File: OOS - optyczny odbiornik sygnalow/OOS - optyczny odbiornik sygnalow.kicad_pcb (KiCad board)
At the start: 2 copper layers, 72 x 79.5 mm, 124 parts, among them J1 Conn_01x02_Pin, J4 Conn_01x02_Socket, J5 Conn_Coaxial, J6 USB_C_Receptacle, Q1 SI2301CDS-T1-GE3, Q2 AOSS32334C, Q3 AOSS32334C, SW1 SW_Rotary_1x8_MP, U1 OPA300AIDBVR, U2 OPA300AIDBVR, U3 AP3015KTR-G1, U4 MCP73831T-2ATI/OT, U5 AP9101CAK6-ANTRG1, U6 AP2126K-ADJTRG1

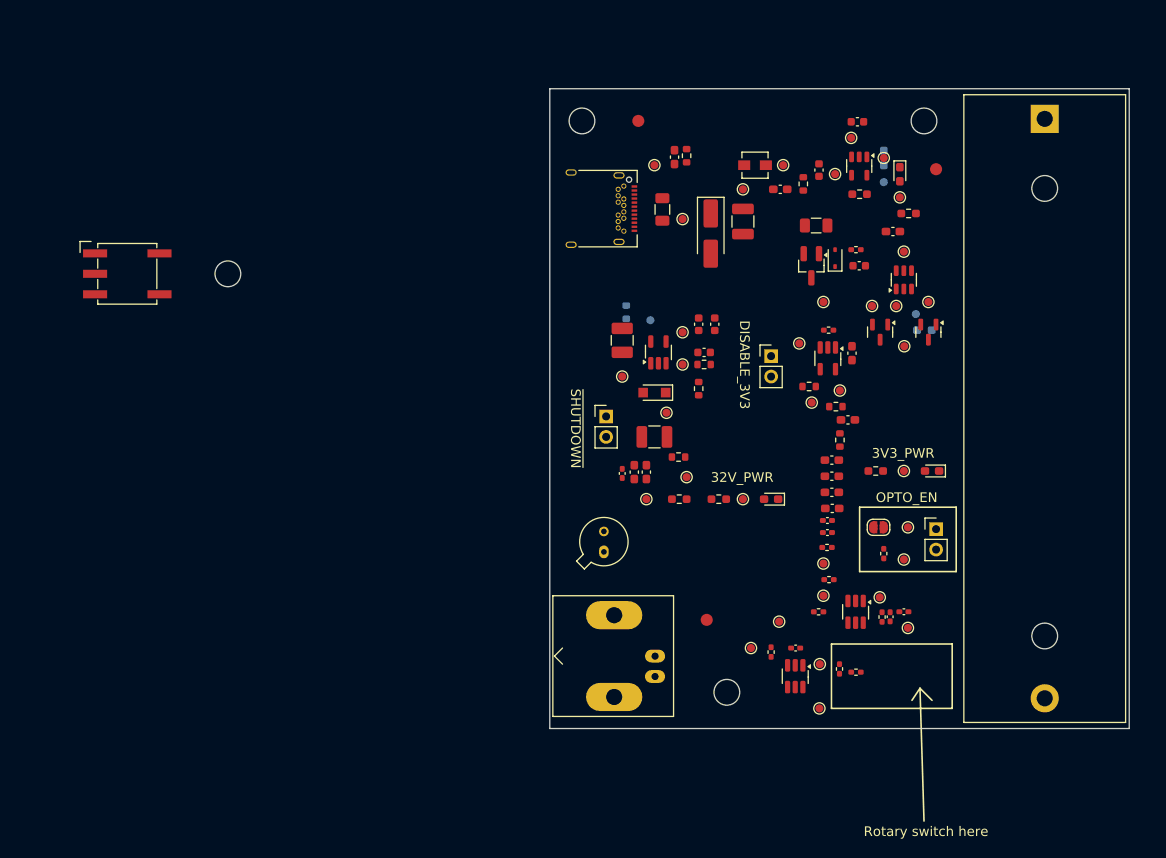
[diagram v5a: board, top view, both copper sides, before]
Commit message: Changing the placement - opamps closer to photodiode, passive components closer to ICs like DCDC converter, Linear 3v3 converter. SHDN resistor moved further away from DCDC and will be routed on the bottom layer
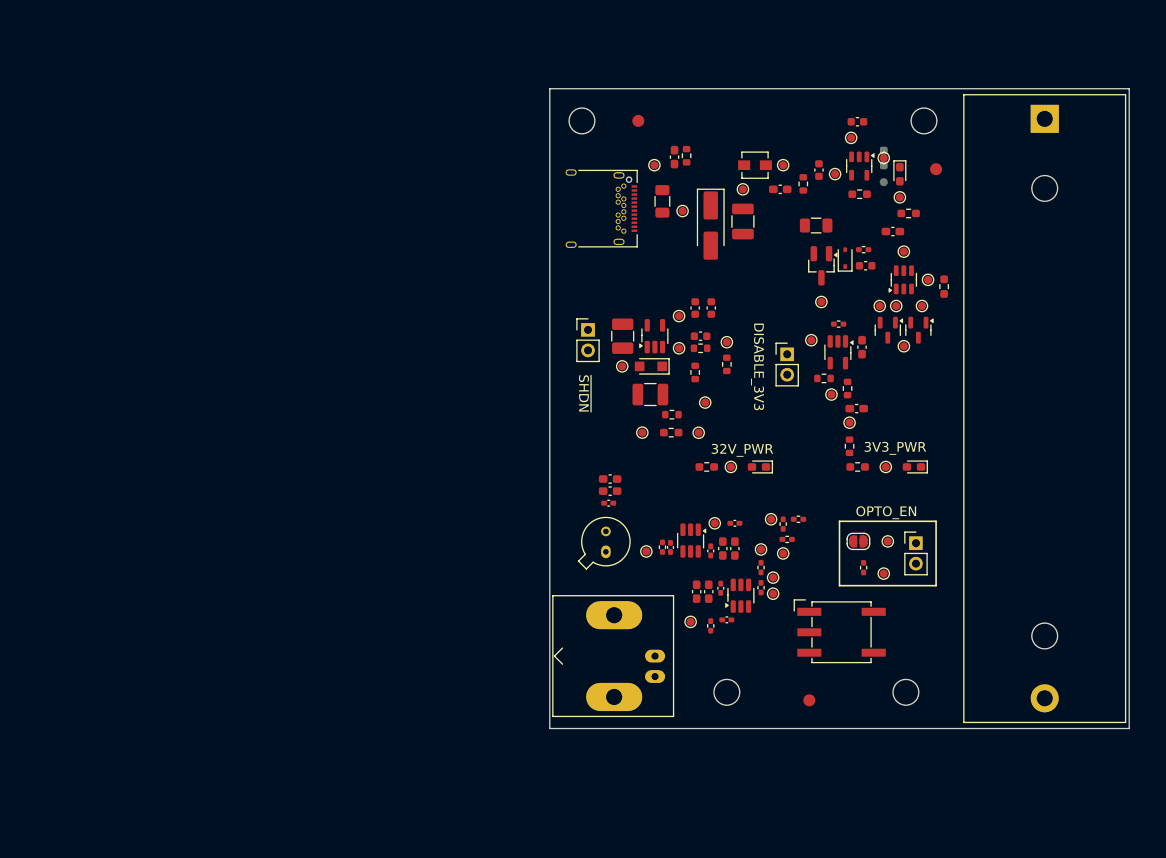
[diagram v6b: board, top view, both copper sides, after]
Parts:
- R13, R17, TP16, TP25: moved to F.Cu
- moved SW1 99.3 mm to (234.7, 95.9)
- moved H3 80.9 mm to (220.4, 103.4)
- moved R8 28.6 mm to (212.4, 85.3)
- moved C10 28.6 mm to (213.4, 85.4)
- moved C11 23.7 mm to (221.4, 82.4)
- moved TP7 22.5 mm to (218.9, 82.4)
- moved U1 22.3 mm to (215.9, 84.5)
- moved H4 22.2 mm to (242.7, 103.4)
- moved C2 22.1 mm to (216.7, 90.9), turned to -90 degrees
- moved TP8 20.7 mm to (224.7, 85.6)
- moved TP6 18.7 mm to (210.4, 85.9)
- moved C4 18.5 mm to (218.2, 90.9), turned to -90 degrees
- moved R9 17.6 mm to (224.7, 87.9), turned to -90 degrees
- moved TP9 17.2 mm to (226.2, 89.1)
- moved C1 16.3 mm to (221.4, 85.5), turned to 90 degrees
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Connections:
- R2 pad 1: Net-(U6-V_{OUT}) -> +3V3
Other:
- board text added: "~{SHDN}"
- board text removed: "~{SHUTDOWN}"

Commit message: repeated push
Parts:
- moved C25 6.58 mm to (207.4, 35.9)
- moved R26 6.55 mm to (208.9, 35.9)
- moved TP38 6.08 mm to (205.4, 36.9)
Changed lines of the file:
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@@
 			(psa4output no)
 			(plot_black_and_white yes)
-			(plotinvisibletext no)
 			(sketchpadsonfab no)
 			(plotpadnumbers no)
@@
 	(footprint "Resistor_SMD:R_0603_1608Metric"
 		(layer "F.Cu")
-		(at 215.42 36.705 90)
+		(at 208.92 35.88 90)
 		(descr "Resistor SMD 0603 (1608 Metric), square (rectangular) end terminal, IPC-7351 nominal, (Body size source: IPC-SM-782 page 72, https://www.pcb-3d.com/wordpress/wp-content/uploads/ipc-sm-782a_amendment_1_and_2.pdf), generated with kicad-footprint-generator")
 		(tags "resistor")
@@
 	(footprint "Capacitor_SMD:C_0603_1608Metric_Pad1.08x0.95mm_HandSolder"
 		(layer "F.Cu")
-		(at 213.92 36.88 90)
+		(at 207.42 35.88 90)
 		(descr "Capacitor SMD 0603 (1608 Metric), square (rectangular) end terminal, IPC-7351 nominal with elongated pad for handsoldering. (Body size source: IPC-SM-782 page 76, https://www.pcb-3d.com/wordpress/wp-content/uploads/ipc-sm-782a_amendment_1_and_2.pdf), generated with kicad-footprint-generator")
 		(tags "capacitor handsolder")
@@
 	(footprint "TestPoint:TestPoint_Pad_D1.0mm"
 		(layer "F.Cu")
-		(at 211.42 37.88)
+		(at 205.42 36.88)
 		(descr "SMD pad as test Point, diameter 1.0mm")
 		(tags "test point SMD pad")

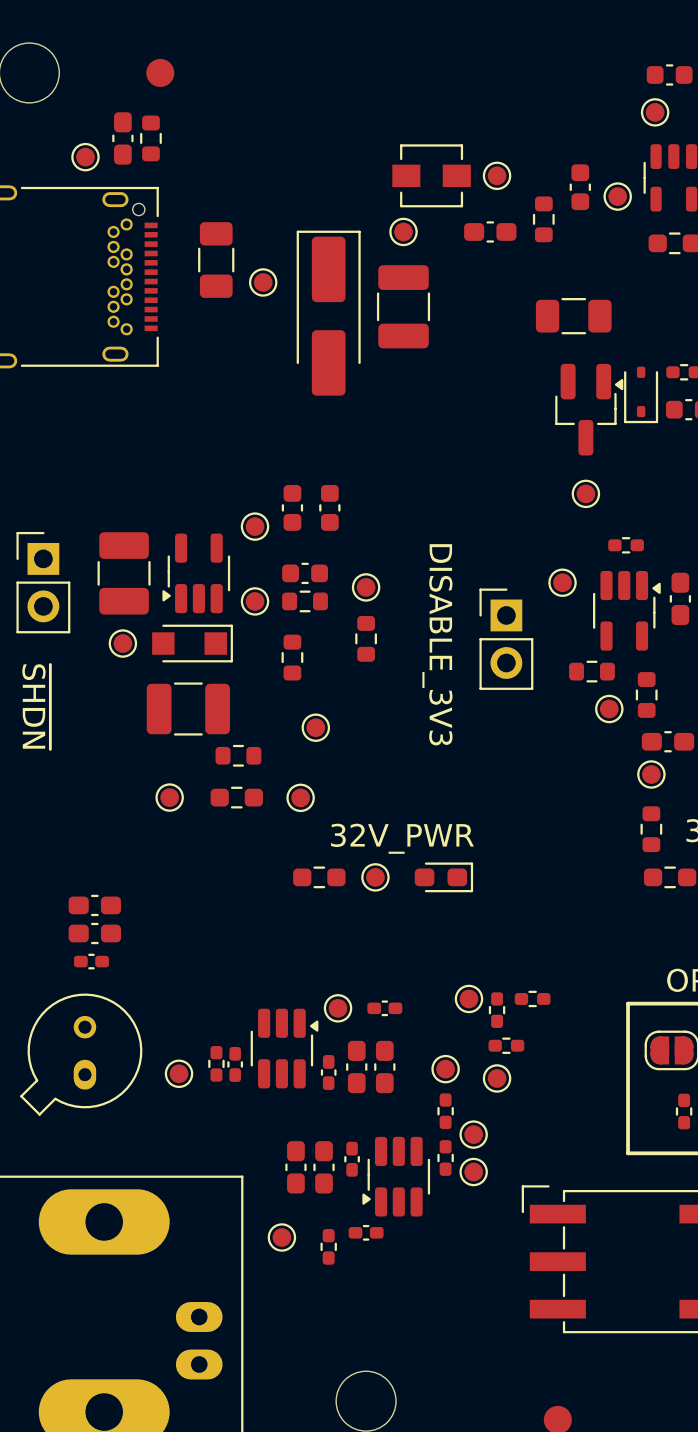
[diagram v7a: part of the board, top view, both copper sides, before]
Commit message: making opto circuit much tighter
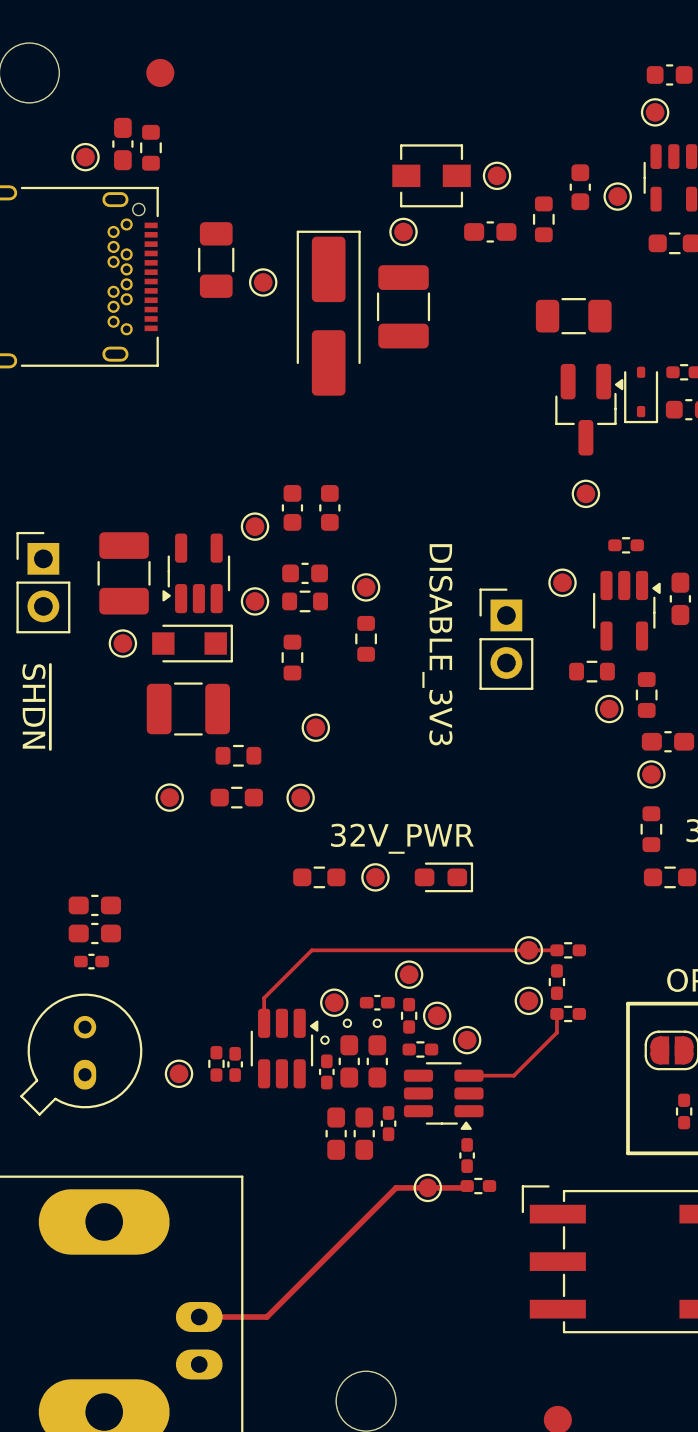
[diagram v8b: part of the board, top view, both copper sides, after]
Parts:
- moved R11 8.63 mm to (226.4, 91.9), turned to 180 degrees
- moved TP11 8.24 mm to (223.7, 92.0)
- moved TP10 7.06 mm to (225.8, 84.1)
- moved C12 6.80 mm to (225.8, 90.2), turned to -90 degrees
- moved TP9 6.64 mm to (224.2, 82.8)
- moved R10 5.95 mm to (223.3, 84.6), turned to 0 degrees
- moved R9 5.46 mm to (222.7, 82.8)
- moved TP8 5.41 mm to (222.7, 80.6)
- moved U2 5.06 mm to (224.6, 86.9), turned to 180 degrees
- moved TP4 4.48 mm to (229.1, 82.0)
- moved TP3 4.12 mm to (229.1, 79.3)
- moved R7 3.71 mm to (231.2, 82.7)
- moved R6 3.53 mm to (230.6, 81.0)
- moved R5 3.22 mm to (231.2, 79.3)
- moved C2 2.80 mm to (218.8, 89.1)
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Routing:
- net /Sekcja_Analogowa/U1_TIA_+: track 0.00 -> 18.1 mm
- net /Sekcja_Analogowa/U2_x10_Out_AC: track 0.00 -> 17.2 mm
- net /Sekcja_Analogowa/U2_x10_+: track 0.00 -> 6.65 mm
- net (no net): vias 0 -> 3
